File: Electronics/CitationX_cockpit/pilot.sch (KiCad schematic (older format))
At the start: 26 parts

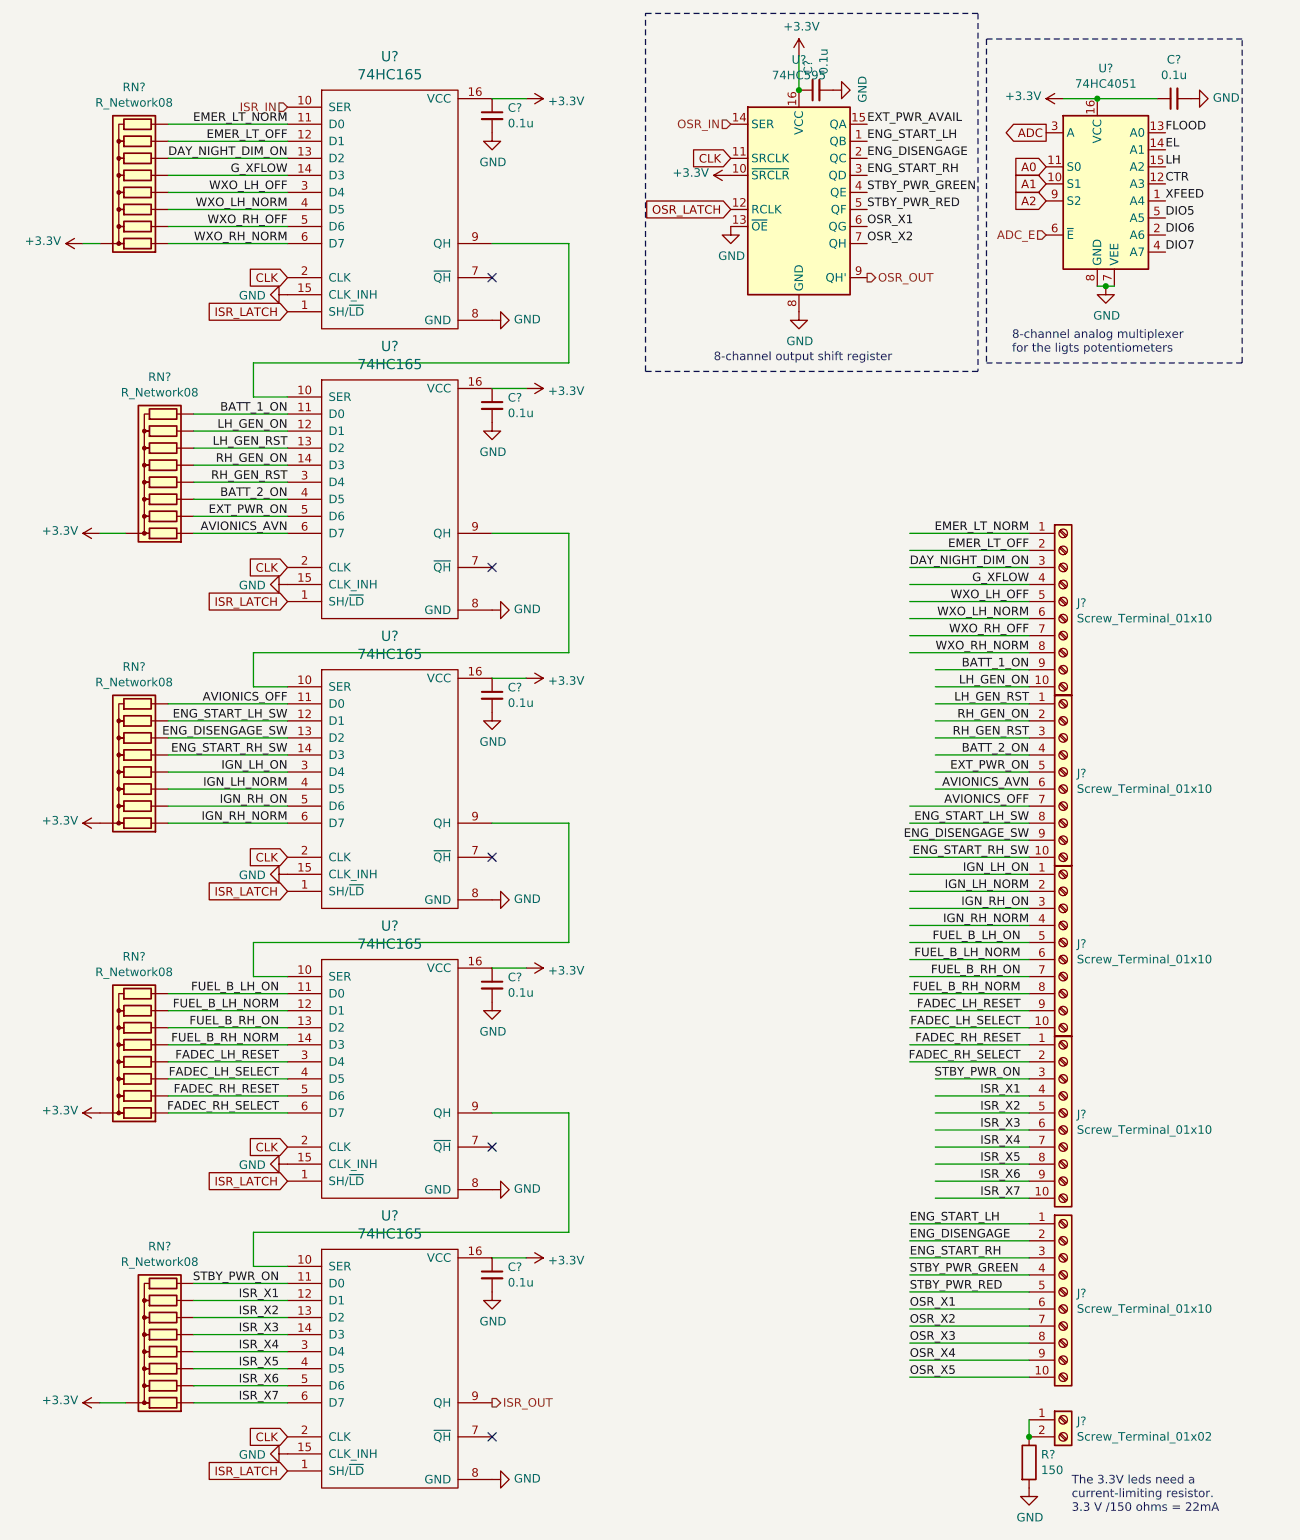
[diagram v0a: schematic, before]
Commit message: Electronics - Misc. works
Continued (and checked board). All connections are probably OK.
Fixed hierarchical pins in APUs (affects all schematics)
Numbered elements for testing schematics
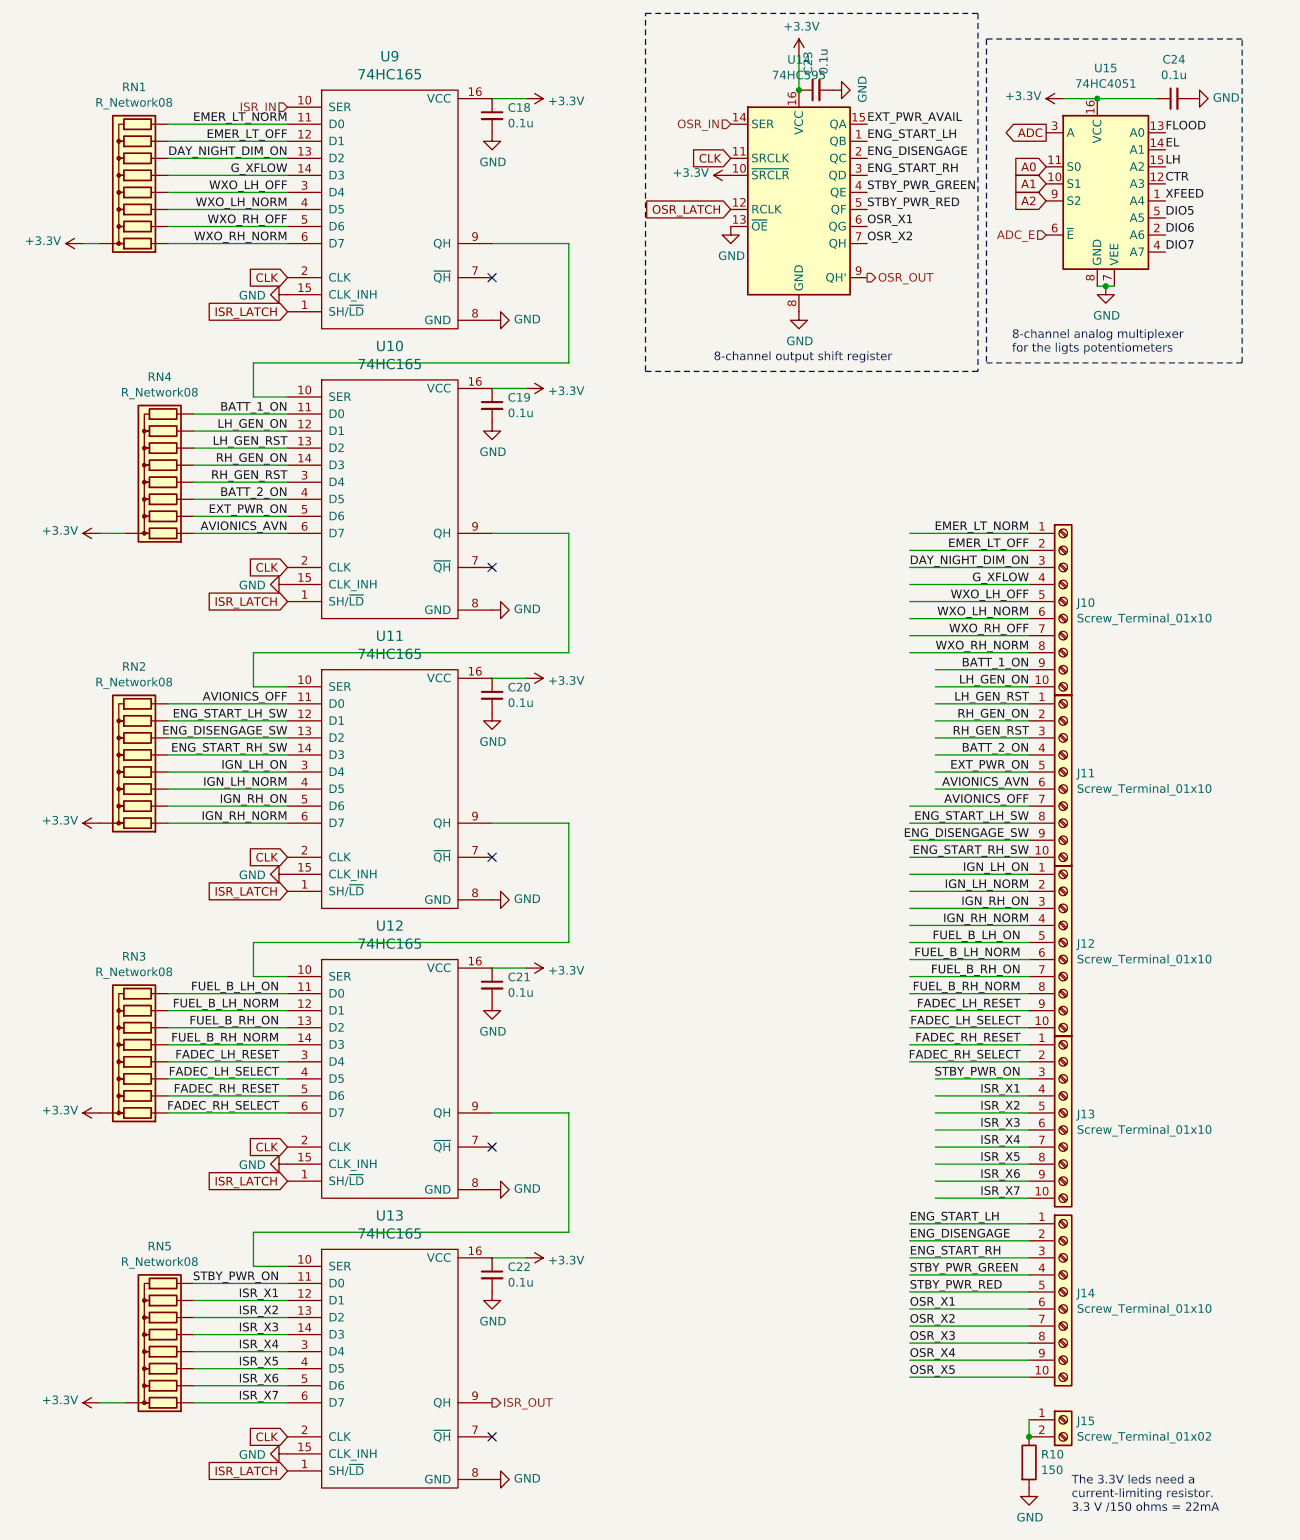
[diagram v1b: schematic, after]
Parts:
- gave numbers to parts that had none: 26
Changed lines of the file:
@@
 P 2750 1650
 AR Path="/5DB5E504" Ref="U?"  Part="1"
-AR Path="/5DB5DCD1/5DB5E504" Ref="U?"  Part="1"
-F 0 "U?" H 2750 2547 60  0000 C CNN
+AR Path="/5DB5DCD1/5DB5E504" Ref="U9"  Part="1"
+F 0 "U9" H 2750 2547 60  0000 C CNN
 F 1 "74HC165" H 2750 2441 60  0000 C CNN
 F 2 "" H 4940 430 60  0001 C CNN
@@
 P 2750 3350
 AR Path="/5DB5FBBC" Ref="U?"  Part="1"
-AR Path="/5DB5DCD1/5DB5FBBC" Ref="U?"  Part="1"
-F 0 "U?" H 2750 4247 60  0000 C CNN
+AR Path="/5DB5DCD1/5DB5FBBC" Ref="U10"  Part="1"
+F 0 "U10" H 2750 4247 60  0000 C CNN
 F 1 "74HC165" H 2750 4141 60  0000 C CNN
 F 2 "" H 4940 2130 60  0001 C CNN
@@
 P 2750 5050
 AR Path="/5DB5FC6F" Ref="U?"  Part="1"
-AR Path="/5DB5DCD1/5DB5FC6F" Ref="U?"  Part="1"
-F 0 "U?" H 2750 5947 60  0000 C CNN
+AR Path="/5DB5DCD1/5DB5FC6F" Ref="U11"  Part="1"
+F 0 "U11" H 2750 5947 60  0000 C CNN
 F 1 "74HC165" H 2750 5841 60  0000 C CNN
 F 2 "" H 4940 3830 60  0001 C CNN
@@
 	1950 4450 2150 4450
 $Comp
-L Device:C_Small C?
+L Device:C_Small C23
 U 1 1 5DB5FD04
 P 5250 950
-F 0 "C?" H 5342 996 50  0000 L CNN
+F 0 "C23" H 5342 996 50  0000 L CNN
 F 1 "0.1u" H 5342 905 50  0000 L CNN
 F 2 "" H 5250 950 50  0001 C CNN
@@
 	5150 950  5150 750
 $Comp
-L Device:C_Small C?
+L Device:C_Small C19
 U 1 1 5DB60100
 P 3350 2800
-F 0 "C?" H 3442 2846 50  0000 L CNN
+F 0 "C19" H 3442 2846 50  0000 L CNN
 F 1 "0.1u" H 3442 2755 50  0000 L CNN
 F 2 "" H 3350 2800 50  0001 C CNN
@@
 	3350 3550 3800 3550
 $Comp
-L Device:C_Small C?
+L Device:C_Small C20
 U 1 1 5DB602E2
 P 3350 4500
-F 0 "C?" H 3442 4546 50  0000 L CNN
+F 0 "C20" H 3442 4546 50  0000 L CNN
 F 1 "0.1u" H 3442 4455 50  0000 L CNN
 F 2 "" H 3350 4500 50  0001 C CNN
@@
 P 2750 6750
 AR Path="/5DB60CE1" Ref="U?"  Part="1"
-AR Path="/5DB5DCD1/5DB60CE1" Ref="U?"  Part="1"
-F 0 "U?" H 2750 7647 60  0000 C CNN
+AR Path="/5DB5DCD1/5DB60CE1" Ref="U12"  Part="1"
+F 0 "U12" H 2750 7647 60  0000 C CNN
 F 1 "74HC165" H 2750 7541 60  0000 C CNN
 F 2 "" H 4940 5530 60  0001 C CNN
@@
 P 2750 8450
 AR Path="/5DB60CFB" Ref="U?"  Part="1"
-AR Path="/5DB5DCD1/5DB60CFB" Ref="U?"  Part="1"
-F 0 "U?" H 2750 9347 60  0000 C CNN
+AR Path="/5DB5DCD1/5DB60CFB" Ref="U13"  Part="1"
+F 0 "U13" H 2750 9347 60  0000 C CNN
 F 1 "74HC165" H 2750 9241 60  0000 C CNN
 F 2 "" H 4940 7230 60  0001 C CNN
@@
 	1950 7850 2150 7850
 $Comp
-L Device:C_Small C?
+L Device:C_Small C21
 U 1 1 5DB60D15
 P 3350 6200
-F 0 "C?" H 3442 6246 50  0000 L CNN
+F 0 "C21" H 3442 6246 50  0000 L CNN
 F 1 "0.1u" H 3442 6155 50  0000 L CNN
 F 2 "" H 3350 6200 50  0001 C CNN
@@
 	3350 6950 3800 6950
 $Comp
-L Device:C_Small C?
+L Device:C_Small C22
 U 1 1 5DB60D25
 P 3350 7900
-F 0 "C?" H 3442 7946 50  0000 L CNN
+F 0 "C22" H 3442 7946 50  0000 L CNN
 F 1 "0.1u" H 3442 7855 50  0000 L CNN
 F 2 "" H 3350 7900 50  0001 C CNN
@@
 ISR_OUT
 $Comp
-L 74xx:74HC595 U?
+L 74xx:74HC595 U14
 U 1 1 5DB61974
 P 5150 1550
-F 0 "U?" H 5150 2328 50  0000 C CNN
+F 0 "U14" H 5150 2328 50  0000 C CNN
 F 1 "74HC595" H 5150 2237 50  0000 C CNN
 F 2 "" H 5150 1550 50  0001 C CNN
@@
 $EndComp
 $Comp
-L Device:C_Small C?
+L Device:C_Small C18
 U 1 1 5DB64E87
 P 3350 1100
-F 0 "C?" H 3442 1146 50  0000 L CNN
+F 0 "C18" H 3442 1146 50  0000 L CNN
 F 1 "0.1u" H 3442 1055 50  0000 L CNN
 F 2 "" H 3350 1100 50  0001 C CNN
@@
 $EndComp
 $Comp
-L Device:R_Network08 RN?
+L Device:R_Network08 RN1
 U 1 1 5DB672BF
 P 1250 1450
-F 0 "RN?" V 1767 1450 50  0000 C CNN
+F 0 "RN1" V 1767 1450 50  0000 C CNN
 F 1 "R_Network08" V 1676 1450 50  0000 C CNN
 F 2 "Resistor_THT:R_Array_SIP9" V 1725 1450 50  0001 C CNN
@@
 $EndComp
 $Comp
-L Device:R_Network08 RN?
+L Device:R_Network08 RN4
 U 1 1 5DB6CDA4
 P 1400 3150
-F 0 "RN?" V 1917 3150 50  0000 C CNN
+F 0 "RN4" V 1917 3150 50  0000 C CNN
 F 1 "R_Network08" V 1826 3150 50  0000 C CNN
 F 2 "Resistor_THT:R_Array_SIP9" V 1875 3150 50  0001 C CNN
@@
 	1200 3550 1050 3550
 $Comp
-L Device:R_Network08 RN?
+L Device:R_Network08 RN2
 U 1 1 5DB6DC27
 P 1250 4850
-F 0 "RN?" V 1767 4850 50  0000 C CNN
+F 0 "RN2" V 1767 4850 50  0000 C CNN
 F 1 "R_Network08" V 1676 4850 50  0000 C CNN
 F 2 "Resistor_THT:R_Array_SIP9" V 1725 4850 50  0001 C CNN
@@
 $EndComp
 $Comp
-L Device:R_Network08 RN?
+L Device:R_Network08 RN3
 U 1 1 5DB6F051
 P 1250 6550
-F 0 "RN?" V 1767 6550 50  0000 C CNN
+F 0 "RN3" V 1767 6550 50  0000 C CNN
 F 1 "R_Network08" V 1676 6550 50  0000 C CNN
 F 2 "Resistor_THT:R_Array_SIP9" V 1725 6550 50  0001 C CNN
@@
 $EndComp
 $Comp
-L Device:R_Network08 RN?
+L Device:R_Network08 RN5
 U 1 1 5DB70CCC
 P 1400 8250
-F 0 "RN?" V 1917 8250 50  0000 C CNN
+F 0 "RN5" V 1917 8250 50  0000 C CNN
 F 1 "R_Network08" V 1826 8250 50  0000 C CNN
 F 2 "Resistor_THT:R_Array_SIP9" V 1875 8250 50  0001 C CNN
@@
 	1200 8650 1050 8650
 $Comp
-L Connector:Screw_Terminal_01x10 J?
+L Connector:Screw_Terminal_01x10 J10
 U 1 1 5DB7391B
 P 6700 3950
-F 0 "J?" H 6780 3942 50  0000 L CNN
+F 0 "J10" H 6780 3942 50  0000 L CNN
 F 1 "Screw_Terminal_01x10" H 6780 3851 50  0000 L CNN
 F 2 "" H 6700 3950 50  0001 C CNN
@@
 ISR_X7
 $Comp
-L Connector:Screw_Terminal_01x10 J?
+L Connector:Screw_Terminal_01x10 J11
 U 1 1 5DCA12CE
 P 6700 4950
-F 0 "J?" H 6780 4942 50  0000 L CNN
+F 0 "J11" H 6780 4942 50  0000 L CNN
 F 1 "Screw_Terminal_01x10" H 6780 4851 50  0000 L CNN
 F 2 "" H 6700 4950 50  0001 C CNN
@@
 $EndComp
 $Comp
-L Connector:Screw_Terminal_01x10 J?
+L Connector:Screw_Terminal_01x10 J12
 U 1 1 5DCA1330
 P 6700 5950
-F 0 "J?" H 6780 5942 50  0000 L CNN
+F 0 "J12" H 6780 5942 50  0000 L CNN
 F 1 "Screw_Terminal_01x10" H 6780 5851 50  0000 L CNN
 F 2 "" H 6700 5950 50  0001 C CNN
@@
 $EndComp
 $Comp
-L Connector:Screw_Terminal_01x10 J?
+L Connector:Screw_Terminal_01x10 J13
 U 1 1 5DCAA24D
 P 6700 6950
-F 0 "J?" H 6780 6942 50  0000 L CNN
+F 0 "J13" H 6780 6942 50  0000 L CNN
 F 1 "Screw_Terminal_01x10" H 6780 6851 50  0000 L CNN
 F 2 "" H 6700 6950 50  0001 C CNN
@@
 ISR_X7
 $Comp
-L Connector:Screw_Terminal_01x02 J?
+L Connector:Screw_Terminal_01x02 J15
 U 1 1 5DCC1605
 P 6700 8750
-F 0 "J?" H 6780 8742 50  0000 L CNN
+F 0 "J15" H 6780 8742 50  0000 L CNN
 F 1 "Screw_Terminal_01x02" H 6780 8651 50  0000 L CNN
 F 2 "" H 6700 8750 50  0001 C CNN
@@
 $EndComp
 $Comp
-L Device:R R?
+L Device:R R10
 U 1 1 5DCC16C8
 P 6500 9000
-F 0 "R?" H 6570 9046 50  0000 L CNN
+F 0 "R10" H 6570 9046 50  0000 L CNN
 F 1 "150" H 6570 8955 50  0000 L CNN
 F 2 "" V 6430 9000 50  0001 C CNN
@@
 $EndComp
 $Comp
-L power:GND #PWR?
+L power:GND #PWR0182
 U 1 1 5DCC175C
 P 6500 9150
-F 0 "#PWR?" H 6500 8900 50  0001 C CNN
+F 0 "#PWR0182" H 6500 8900 50  0001 C CNN
 F 1 "GND" H 6505 8977 50  0000 C CNN
 F 2 "" H 6500 9150 50  0001 C CNN
@@
 Connection ~ 6500 8850
 $Comp
-L Connector:Screw_Terminal_01x10 J?
+L Connector:Screw_Terminal_01x10 J14
 U 1 1 5DCCB96C
 P 6700 8000
-F 0 "J?" H 6780 7992 50  0000 L CNN
+F 0 "J14" H 6780 7992 50  0000 L CNN
 F 1 "Screw_Terminal_01x10" H 6780 7901 50  0000 L CNN
 F 2 "" H 6700 8000 50  0001 C CNN
@@
 	5800 8300 6500 8300
 $Comp
-L 74xx:74HC4051 U?
+L 74xx:74HC4051 U15
 U 1 1 5DD02C29
 P 6900 1500
-F 0 "U?" H 6950 2178 50  0000 C CNN
+F 0 "U15" H 6950 2178 50  0000 C CNN
 F 1 "74HC4051" H 6950 2087 50  0000 C CNN
 F 2 "" H 6900 1100 50  0001 C CNN
@@
 	6900 2100 6950 2100
 $Comp
-L power:GND #PWR?
+L power:GND #PWR0183
 U 1 1 5DD02C3E
 P 6950 2100
-F 0 "#PWR?" H 6950 1850 50  0001 C CNN
+F 0 "#PWR0183" H 6950 1850 50  0001 C CNN
 F 1 "GND" H 6955 1927 50  0000 C CNN
 F 2 "" H 6950 2100 50  0001 C CNN
@@
 	6950 2100 7000 2100
 $Comp
-L Device:C_Small C?
+L Device:C_Small C24
 U 1 1 5DD02C46
 P 7350 1000
-F 0 "C?" V 7579 1000 50  0000 C CNN
+F 0 "C24" V 7579 1000 50  0000 C CNN
 F 1 "0.1u" V 7488 1000 50  0000 C CNN
 F 2 "" H 7350 1000 50  0001 C CNN
@@
 	6900 1000 7250 1000
 $Comp
-L power:GND #PWR?
+L power:GND #PWR0184
 U 1 1 5DD02C4E
 P 7450 1000
-F 0 "#PWR?" H 7450 750 50  0001 C CNN
+F 0 "#PWR0184" H 7450 750 50  0001 C CNN
 F 1 "GND" V 7455 872 50  0000 R CNN
 F 2 "" H 7450 1000 50  0001 C CNN
@@
 $EndComp
 $Comp
-L power:+3.3V #PWR?
+L power:+3.3V #PWR0185
 U 1 1 5DD02C54
 P 6700 1000
-F 0 "#PWR?" H 6700 850 50  0001 C CNN
+F 0 "#PWR0185" H 6700 850 50  0001 C CNN
 F 1 "+3.3V" V 6715 1128 50  0000 L CNN
 F 2 "" H 6700 1000 50  0001 C CNN
